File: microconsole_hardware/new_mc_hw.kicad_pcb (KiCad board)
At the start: 2 copper layers, 161 x 96.5 mm, 107 parts, among them J2 USB_C_Receptacle_USB2.0_16P, SW1 SW_Nidec_CAS-120A1, SW17 Joystick, SW18 Joystick, SW33 TL3301NF160QG, SW34 TL3301NF160QG, SW35 TL3301NF160QG, SW36 TL3301NF160QG, SW37 TL3301NF160QG, SW38 TL3301NF160QG, SW39 TL3301NF160QG, SW40 TL3301NF160QG, SW41 TL3301NF160QG, SW42 TL3301NF160QG, SW43 TL3301NF160QG, SW44 TL3301NF160QG, SW45 TL3301NF160QG, SW46 TL3301NF160QG, U15 ADS7828E/2K5, U16 MCP23017-E/SO, U20 PCM5102APWR, U21 PAM8302AADCR, U22 PAM8406DR, U23 S2B-PH-K-S, U6 MCP73833_MSOP

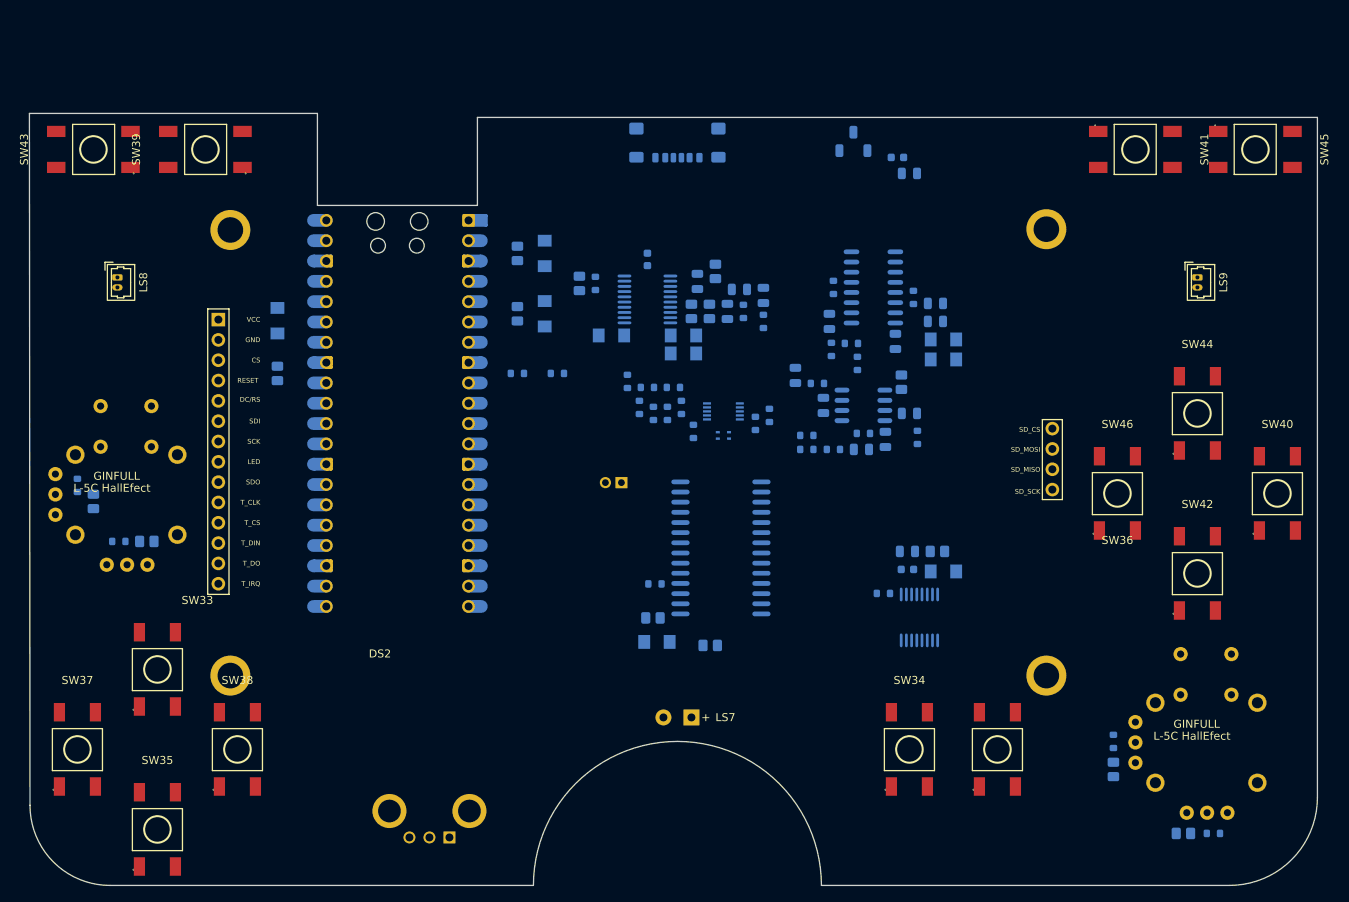
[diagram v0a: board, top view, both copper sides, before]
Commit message: recover lost pages
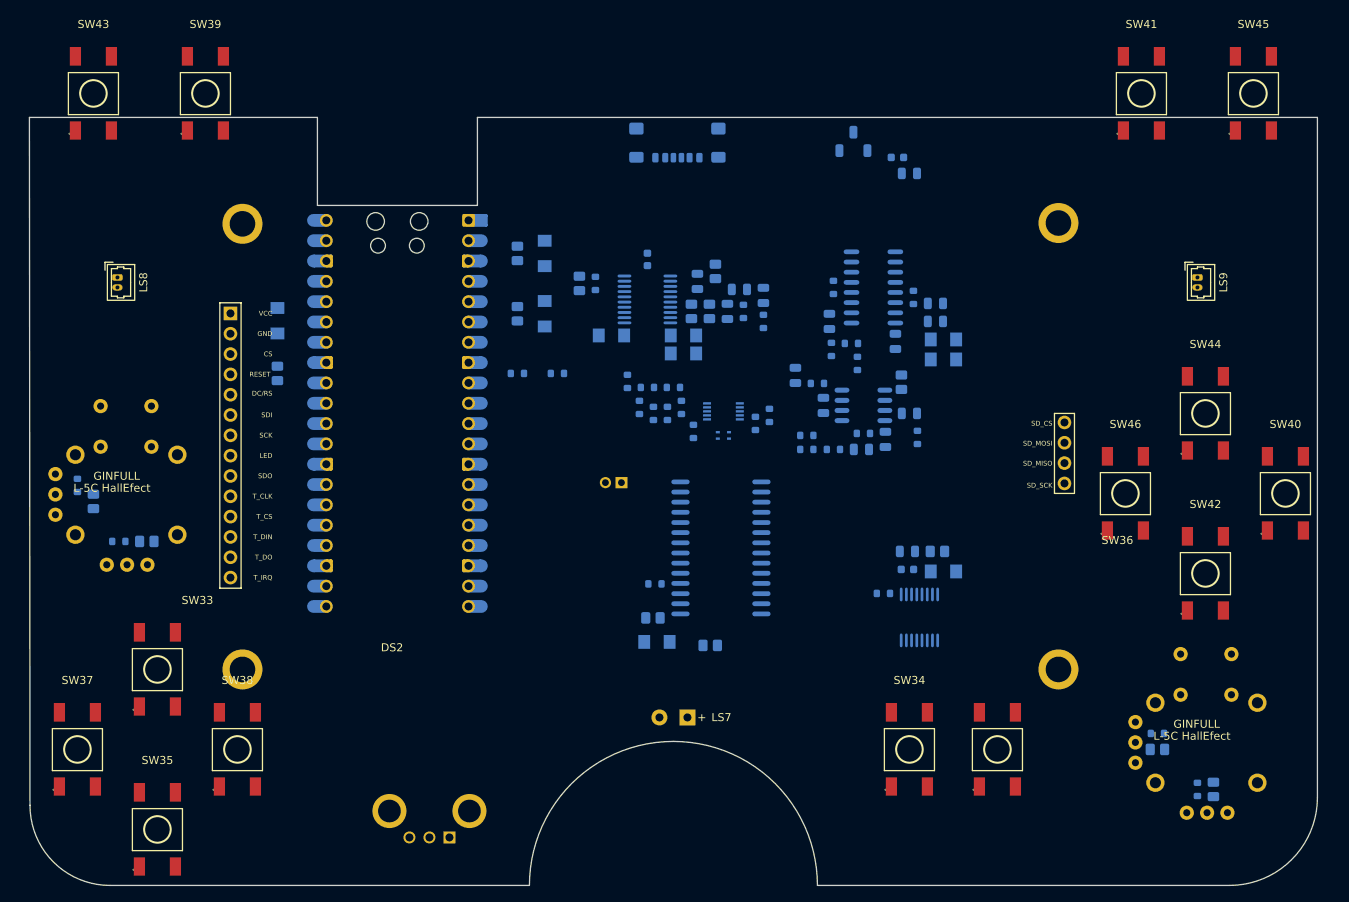
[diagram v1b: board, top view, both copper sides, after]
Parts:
- moved SW41 7.04 mm to (208.0, 55.0), turned to 0 degrees
- moved SW45 7.00 mm to (222.0, 55.0), turned to 0 degrees
- moved SW39 7.00 mm to (91.0, 55.0), turned to 0 degrees
- moved SW43 7.00 mm to (77.0, 55.0), turned to 0 degrees
- moved C78 6.66 mm to (217.0, 142.0), turned to 90 degrees
- moved C79 6.04 mm to (210.0, 137.0), turned to 0 degrees
- moved R47 5.85 mm to (215.0, 142.0), turned to -90 degrees
- moved R48 5.59 mm to (210.0, 135.0), turned to 180 degrees
- moved DS2 1.70 mm to (92.6, 130.0)
- moved SW40 1.00 mm to (226.0, 105.0)
- moved SW42 1.00 mm to (216.0, 115.0)
- moved SW44 1.00 mm to (216.0, 95.0)
- moved SW46 1.00 mm to (206.0, 105.0)
- moved LS7 0.50 mm to (151.2, 133.0)
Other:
- board size 161 x 96.5 mm -> 161 x 96 mm
